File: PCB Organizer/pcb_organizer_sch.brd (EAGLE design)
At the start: 160 x 100 mm, 3 parts, among them U1 ARDUINO_NANO, U2 V8FR-II

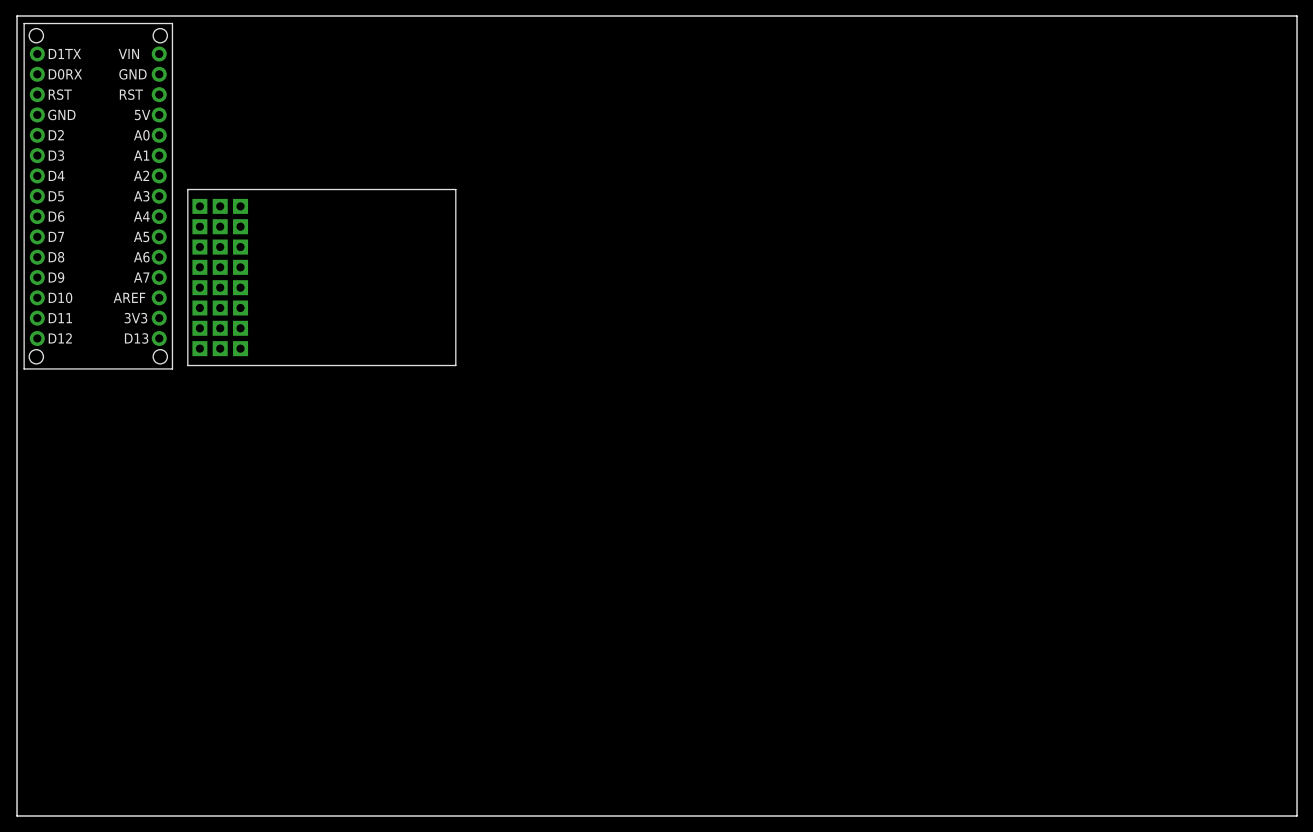
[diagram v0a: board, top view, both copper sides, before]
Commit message: Added Pololu TB67 motor driver to the library, board, and schematic
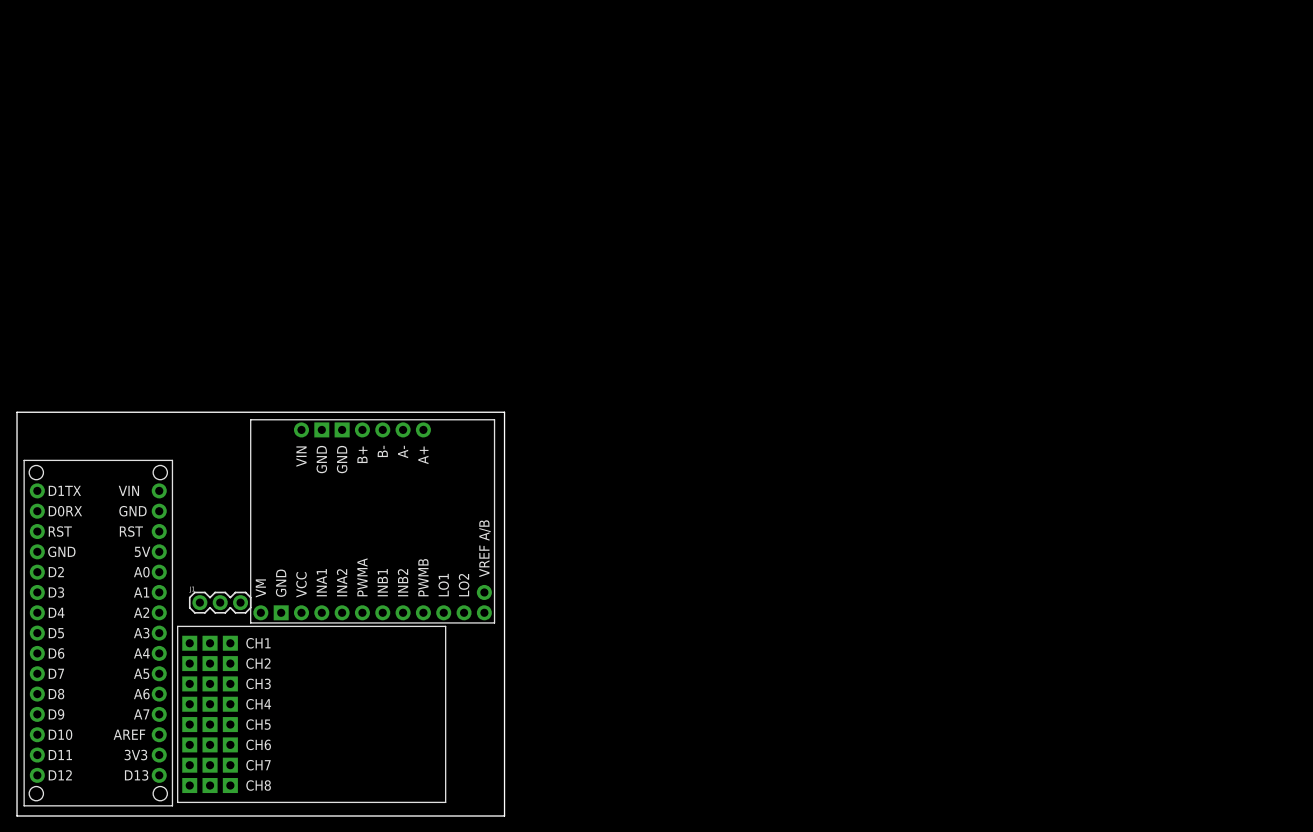
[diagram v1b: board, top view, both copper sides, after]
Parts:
- added J1: 455-1750-1-ND, SparkFun-Connectors:1X03
- added U3: POLOLU_TB67, CUCombatBots:POLOLU_TB67
- moved U2 54.6 mm to (36.8, 12.7)
- moved U1 54.6 mm to (10.2, 22.9)
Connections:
- net 5V: now also J1.2
- net CH1: now also J1.1
- net GND: now also J1.3
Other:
- board size 160 x 100 mm -> 60.9 x 50.5 mm
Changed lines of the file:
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@@
 <drawing>
 <settings>
-<setting alwaysvectorfont="no"/>
+<setting alwaysvectorfont="yes"/>
 <setting verticaltext="up"/>
 </settings>
@@
 </layers>
 <board>
+<fusionsync huburn="a.cGVyc29uYWw6dWUyYTQwMmQx" projecturn="a.cGVyc29uYWw6dWUyYTQwMmQxIzIwMTkwNjIwMTk5ODA3OTMx" f3durn="urn:adsk.wipprod:dm.lineage:vlrF4oSVT-SXZak__tytiQ" pcbguid="f8ca07a6-3519-48d8-a1f2-b6a89162f8ee" lastpulledtime="" lastsyncedchangeguid="96adb79c-92be-0b7b-3d07-4bf4f0737942"/>
 <plain>
-<wire x1="0" y1="0" x2="160" y2="0" width="0" layer="20"/>
-<wire x1="160" y1="0" x2="160" y2="100" width="0" layer="20"/>
-<wire x1="160" y1="100" x2="0" y2="100" width="0" layer="20"/>
-<wire x1="0" y1="100" x2="0" y2="0" width="0" layer="20"/>
+<wire x1="0" y1="0" x2="60.94" y2="0" width="0" layer="20"/>
+<wire x1="60.94" y1="0" x2="60.94" y2="50.47" width="0" layer="20"/>
+<wire x1="60.94" y1="50.47" x2="0" y2="50.47" width="0" layer="20"/>
+<wire x1="0" y1="50.47" x2="0" y2="0" width="0" layer="20"/>
 </plain>
 <attributes>
@@
 <attribute name="REV" value="" x="0" y="0" size="1.778" layer="27" display="off"/>
 </element>
-<element name="U1" library="CUCombatBots" package="ARDUINO_NANO" value="ARDUINO_NANO" x="10.16" y="77.47" smashed="yes"/>
-<element name="U2" library="CUCombatBots" package="V8FR-II" value="V8FR-II" x="38.1" y="67.31" smashed="yes" rot="R90"/>
+<element name="U1" library="CUCombatBots" package="ARDUINO_NANO" value="ARDUINO_NANO" x="10.16" y="22.86" smashed="yes"/>
+<element name="U2" library="CUCombatBots" package="V8FR-II" value="V8FR-II" x="36.83" y="12.7" smashed="yes" rot="R90"/>
+<element name="J1" library="SparkFun-Connectors" package="1X03" value="455-1750-1-ND" x="22.86" y="26.67" smashed="yes">
+<attribute name="NAME" x="21.59" y="28.067" size="0.6096" layer="25" font="vector" ratio="20"/>
+<attribute name="PROD_ID" value="XXX-00000" x="22.86" y="26.67" size="1.778" layer="27" display="off"/>
+<attribute name="VALUE" x="21.59" y="24.638" size="0.6096" layer="27" font="vector" ratio="20"/>
+</element>
+<element name="U3" library="CUCombatBots" package="POLOLU_TB67" value="POLOLU_TB67" x="44.45" y="36.83" smashed="yes" rot="R90"/>
 </elements>
 <signals>
@@
 <contactref element="U2" pad="VIN_8"/>
 <contactref element="U1" pad="5V"/>
-<wire x1="25.4" y1="76.2" x2="17.78" y2="87.63" width="0" layer="19" extent="1-1"/>
-<wire x1="25.4" y1="73.66" x2="25.4" y2="76.2" width="0" layer="19" extent="1-1"/>
-<wire x1="25.4" y1="71.12" x2="25.4" y2="73.66" width="0" layer="19" extent="1-1"/>
-<wire x1="25.4" y1="68.58" x2="25.4" y2="71.12" width="0" layer="19" extent="1-1"/>
-<wire x1="25.4" y1="66.04" x2="25.4" y2="68.58" width="0" layer="19" extent="1-1"/>
-<wire x1="25.4" y1="63.5" x2="25.4" y2="66.04" width="0" layer="19" extent="1-1"/>
-<wire x1="25.4" y1="60.96" x2="25.4" y2="63.5" width="0" layer="19" extent="1-1"/>
-<wire x1="25.4" y1="58.42" x2="25.4" y2="60.96" width="0" layer="19" extent="1-1"/>
+<contactref element="J1" pad="2"/>
+<wire x1="24.13" y1="21.59" x2="17.78" y2="33.02" width="0" layer="19" extent="1-1"/>
+<wire x1="24.13" y1="19.05" x2="24.13" y2="21.59" width="0" layer="19" extent="1-1"/>
+<wire x1="24.13" y1="16.51" x2="24.13" y2="19.05" width="0" layer="19" extent="1-1"/>
+<wire x1="24.13" y1="13.97" x2="24.13" y2="16.51" width="0" layer="19" extent="1-1"/>
+<wire x1="24.13" y1="11.43" x2="24.13" y2="13.97" width="0" layer="19" extent="1-1"/>
+<wire x1="24.13" y1="8.89" x2="24.13" y2="11.43" width="0" layer="19" extent="1-1"/>
+<wire x1="24.13" y1="6.35" x2="24.13" y2="8.89" width="0" layer="19" extent="1-1"/>
+<wire x1="24.13" y1="3.81" x2="24.13" y2="6.35" width="0" layer="19" extent="1-1"/>
+<wire x1="25.4" y1="26.67" x2="24.13" y2="3.81" width="0" layer="19" extent="1-1"/>
 </signal>
 <signal name="CH1">
 <contactref element="U2" pad="1"/>
 <contactref element="U1" pad="D6"/>
-<wire x1="27.94" y1="76.2" x2="2.54" y2="74.93" width="0" layer="19" extent="1-1"/>
+<contactref element="J1" pad="1"/>
+<wire x1="2.54" y1="20.32" x2="26.67" y2="21.59" width="0" layer="19" extent="1-1"/>
+<wire x1="22.86" y1="26.67" x2="2.54" y2="20.32" width="0" layer="19" extent="1-1"/>
 </signal>
 <signal name="CH2">
 <contactref element="U2" pad="2"/>
 <contactref element="U1" pad="D7"/>
-<wire x1="27.94" y1="73.66" x2="2.54" y2="72.39" width="0" layer="19" extent="1-1"/>
+<wire x1="26.67" y1="19.05" x2="2.54" y2="17.78" width="0" layer="19" extent="1-1"/>
 </signal>
 <signal name="CH3">
 <contactref element="U2" pad="3"/>
 <contactref element="U1" pad="D8"/>
-<wire x1="27.94" y1="71.12" x2="2.54" y2="69.85" width="0" layer="19" extent="1-1"/>
+<wire x1="26.67" y1="16.51" x2="2.54" y2="15.24" width="0" layer="19" extent="1-1"/>
 </signal>
 <signal name="CH4">
 <contactref element="U2" pad="4"/>
 <contactref element="U1" pad="D9"/>
-<wire x1="27.94" y1="68.58" x2="2.54" y2="67.31" width="0" layer="19" extent="1-1"/>
+<wire x1="26.67" y1="13.97" x2="2.54" y2="12.7" width="0" layer="19" extent="1-1"/>
 </signal>
 <signal name="CH5">
 <contactref element="U2" pad="5"/>
 <contactref element="U1" pad="D10"/>
-<wire x1="27.94" y1="66.04" x2="2.54" y2="64.77" width="0" layer="19" extent="1-1"/>
+<wire x1="26.67" y1="11.43" x2="2.54" y2="10.16" width="0" layer="19" extent="1-1"/>
 </signal>
 <signal name="CH6">
 <contactref element="U2" pad="6"/>
 <contactref element="U1" pad="D11"/>
-<wire x1="27.94" y1="63.5" x2="2.54" y2="62.23" width="0" layer="19" extent="1-1"/>
+<wire x1="26.67" y1="8.89" x2="2.54" y2="7.62" width="0" layer="19" extent="1-1"/>
 </signal>
 <signal name="CH7">
 <contactref element="U2" pad="7"/>
 <contactref element="U1" pad="D12"/>
-<wire x1="27.94" y1="60.96" x2="2.54" y2="59.69" width="0" layer="19" extent="1-1"/>
+<wire x1="26.67" y1="6.35" x2="2.54" y2="5.08" width="0" layer="19" extent="1-1"/>
 </signal>
 <signal name="CH8">
 <contactref element="U2" pad="8"/>
 <contactref element="U1" pad="D13"/>
-<wire x1="17.78" y1="59.69" x2="27.94" y2="58.42" width="0" layer="19" extent="1-1"/>
+<wire x1="17.78" y1="5.08" x2="26.67" y2="3.81" width="0" layer="19" extent="1-1"/>
 </signal>
 <signal name="GND">
@@
 <contactref element="U1" pad="GND"/>
 <contactref element="U1" pad="GND_@16"/>
-<wire x1="2.54" y1="87.63" x2="17.78" y2="92.71" width="0" layer="19" extent="1-1"/>
-<wire x1="22.86" y1="76.2" x2="2.54" y2="87.63" width="0" layer="19" extent="1-1"/>
+<contactref element="J1" pad="3"/>
+<wire x1="2.54" y1="33.02" x2="17.78" y2="38.1" width="0" layer="19" extent="1-1"/>
+<wire x1="21.59" y1="21.59" x2="17.78" y2="38.1" width="0" layer="19" extent="1-1"/>
+<wire x1="27.94" y1="26.67" x2="21.59" y2="3.81" width="0" layer="19" extent="1-1"/>
 </signal>
 </signals>
@@
 </board>
 </drawing>
+<compatibility>
+<note version="8.3" severity="warning">
+Since Version 8.3, EAGLE supports Fusion synchronisation.
+This feature will not be available in this version and saving
+the document will break the link to the Fusion PCB feature.
+</note>
+</compatibility>
 </eagle>

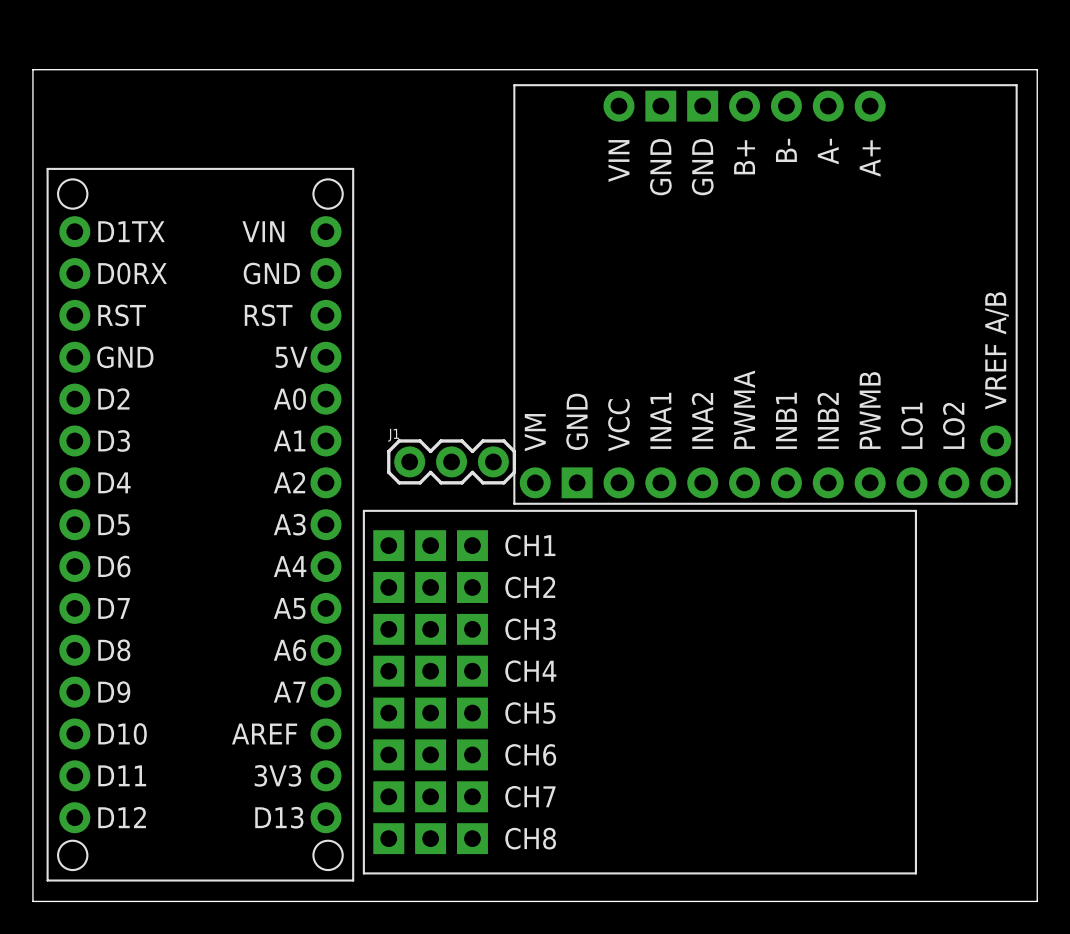
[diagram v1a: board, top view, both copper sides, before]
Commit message: Finished Schematic and laid out the board. No routing
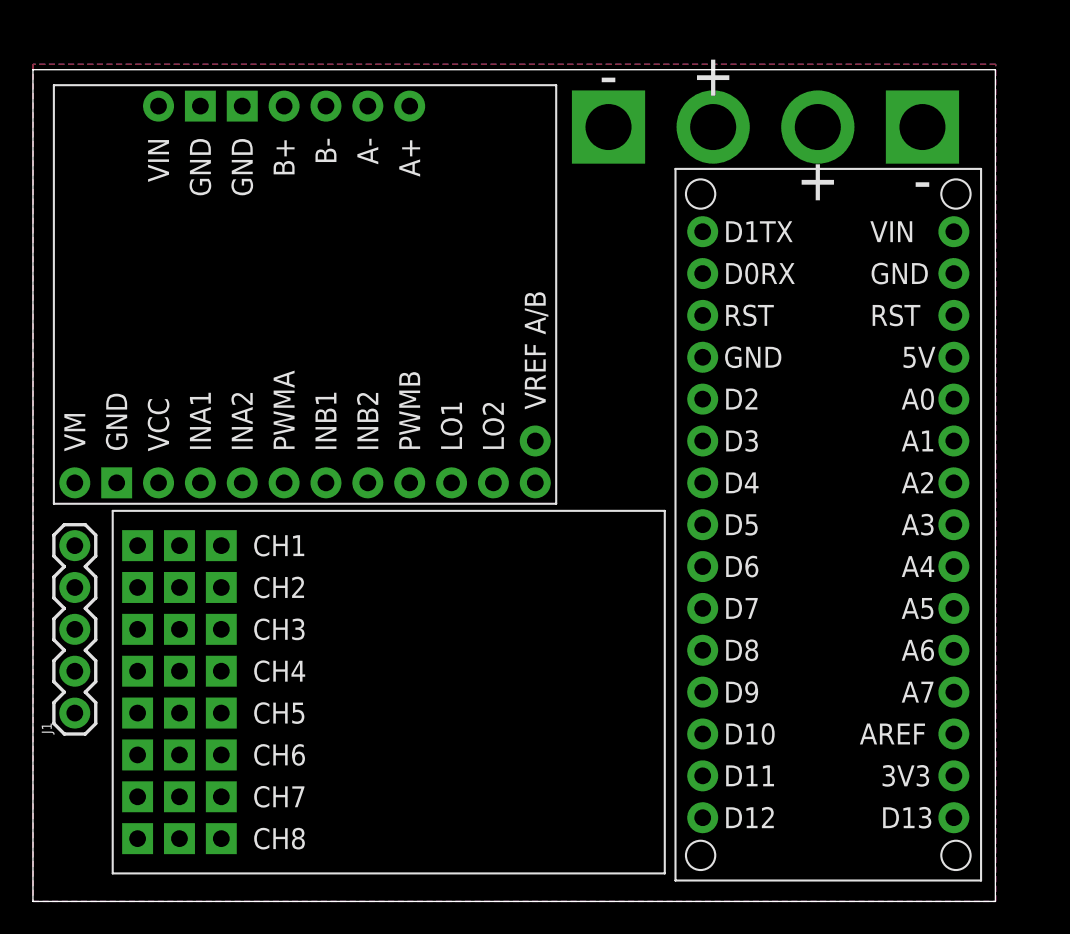
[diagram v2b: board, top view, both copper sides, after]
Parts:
- added J2, J3: BATT, CUCombatBots:CONN_2_10AUG
- J1: device SparkFun-Connectors:1X03 -> SparkFun-Connectors:1X05
- moved U1 38.1 mm to (48.3, 22.9)
- moved U3 27.9 mm to (16.5, 36.8)
- moved J1 25.4 mm to (2.54, 11.4), turned to 90 degrees
- moved U2 15.2 mm to (21.6, 12.7)
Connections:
- new net LEFT_IN_1: U1.D2, U3.INA1
- new net LEFT_IN_2: U1.D3, U3.INA2
- new net LEFT_PWM: U1.D10, U3.PWMA
- new net RIGHT_IN_1: U1.D4, U3.INB1
- new net RIGHT_IN_2: U1.D5, U3.INB2
- new net RIGHT_PWM: U1.D11, U3.PWMB
- new net V_BATT: J1.5, J3.-, U1.VIN, U3.VIN
- new net V_BATT_RAW: J2.+, J3.+
- net 5V: now also J1.4, U3.VCC; no longer J1.2
- net CH1: no longer J1.1
- net CH3: now also J1.3
- net CH5: now also U1.D12; no longer U1.D10
- net CH6: now also U1.D13; no longer U1.D11
- net CH7: no longer U1.D12
- net CH8: no longer U1.D13
- net GND: now also J1.1, J1.2, J2.-, U3.GND, U3.GND@14, U3.GND@15; no longer J1.3
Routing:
- added copper zone on layer 16, net GND
- added copper zone on layer 1, net V_BATT
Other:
- board size 60.9 x 50.5 mm -> 58.4 x 50.5 mm

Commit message: Finished routing
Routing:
- net 5V: track 0.00 -> 103.3 mm
- net CH6: track 0.00 -> 47.1 mm
- net CH3: track 0.00 -> 39.6 mm
- net LEFT_IN_1: track 0.00 -> 33.6 mm
- net CH5: track 0.00 -> 31.8 mm
- net LEFT_PWM: track 0.00 -> 31.7 mm, vias 0 -> 1
- net LEFT_IN_2: track 0.00 -> 31.1 mm
- net CH4: track 0.00 -> 29.7 mm
- net CH2: track 0.00 -> 29.7 mm
- net CH1: track 0.00 -> 29.7 mm
- net RIGHT_PWM: track 0.00 -> 29.6 mm
- net RIGHT_IN_1: track 0.00 -> 26.0 mm
- net RIGHT_IN_2: track 0.00 -> 21.4 mm
- net V_BATT_RAW: track 0.00 -> 12.7 mm

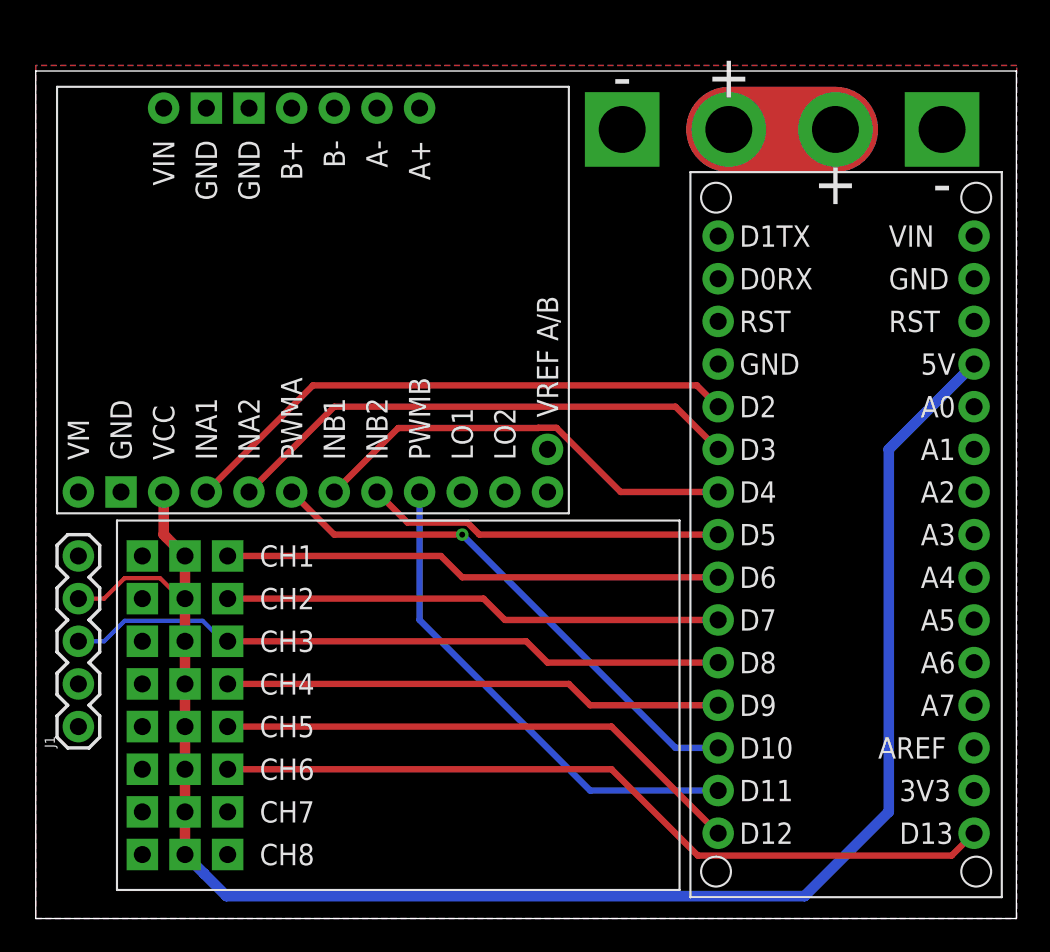
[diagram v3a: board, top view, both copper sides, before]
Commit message: Increased polygon connection trace thickness
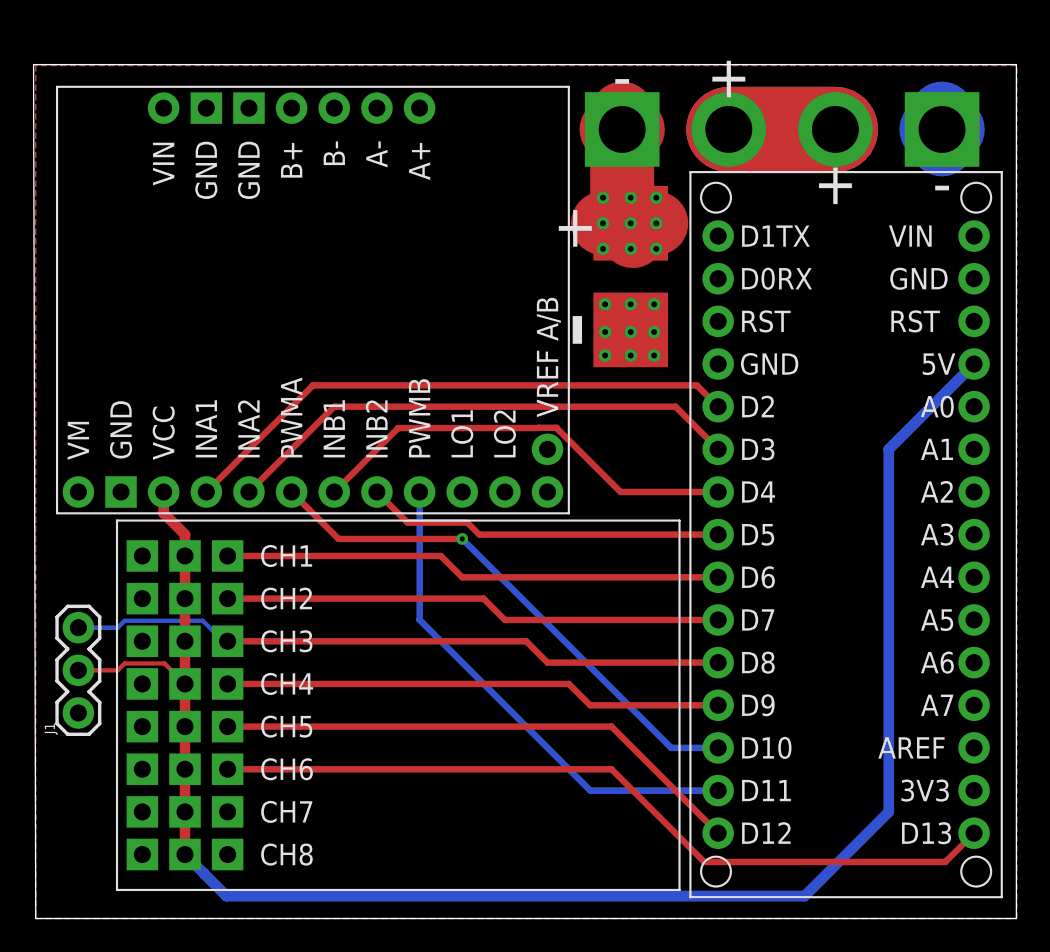
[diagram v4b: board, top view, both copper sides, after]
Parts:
- added J4: BATTPAD, CUCombatBots:BATT_PADS
- J1: device SparkFun-Connectors:1X05 -> SparkFun-Connectors:1X03
- moved J1 0.81 mm to (2.54, 12.2)
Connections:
- net 5V: now also J1.2; no longer J1.4
- net GND: now also J4.-; no longer J1.2
- net V_BATT: now also J4.+; no longer J1.5
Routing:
- net V_BATT: track 0.00 -> 12.0 mm, vias 0 -> 9
- net GND: track 0.00 -> 3.10 mm, vias 0 -> 9
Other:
- board size 58.4 x 50.5 mm -> 58.5 x 50.9 mm
